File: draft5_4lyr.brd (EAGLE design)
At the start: 120 x 100 mm, 193 parts, among them Q1 Si2333, Q2 2N7002, Q3 2N7002, Q4 2N7002, Q5 2N7002, Q6 2N7002, Q7 2N7002, SW1 TOUCH_PAD-CIRCLE-15MM, SW10 TOUCH_PAD-CIRCLE-15MM, SW4 TOUCH_PAD-CIRCLE-15MM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

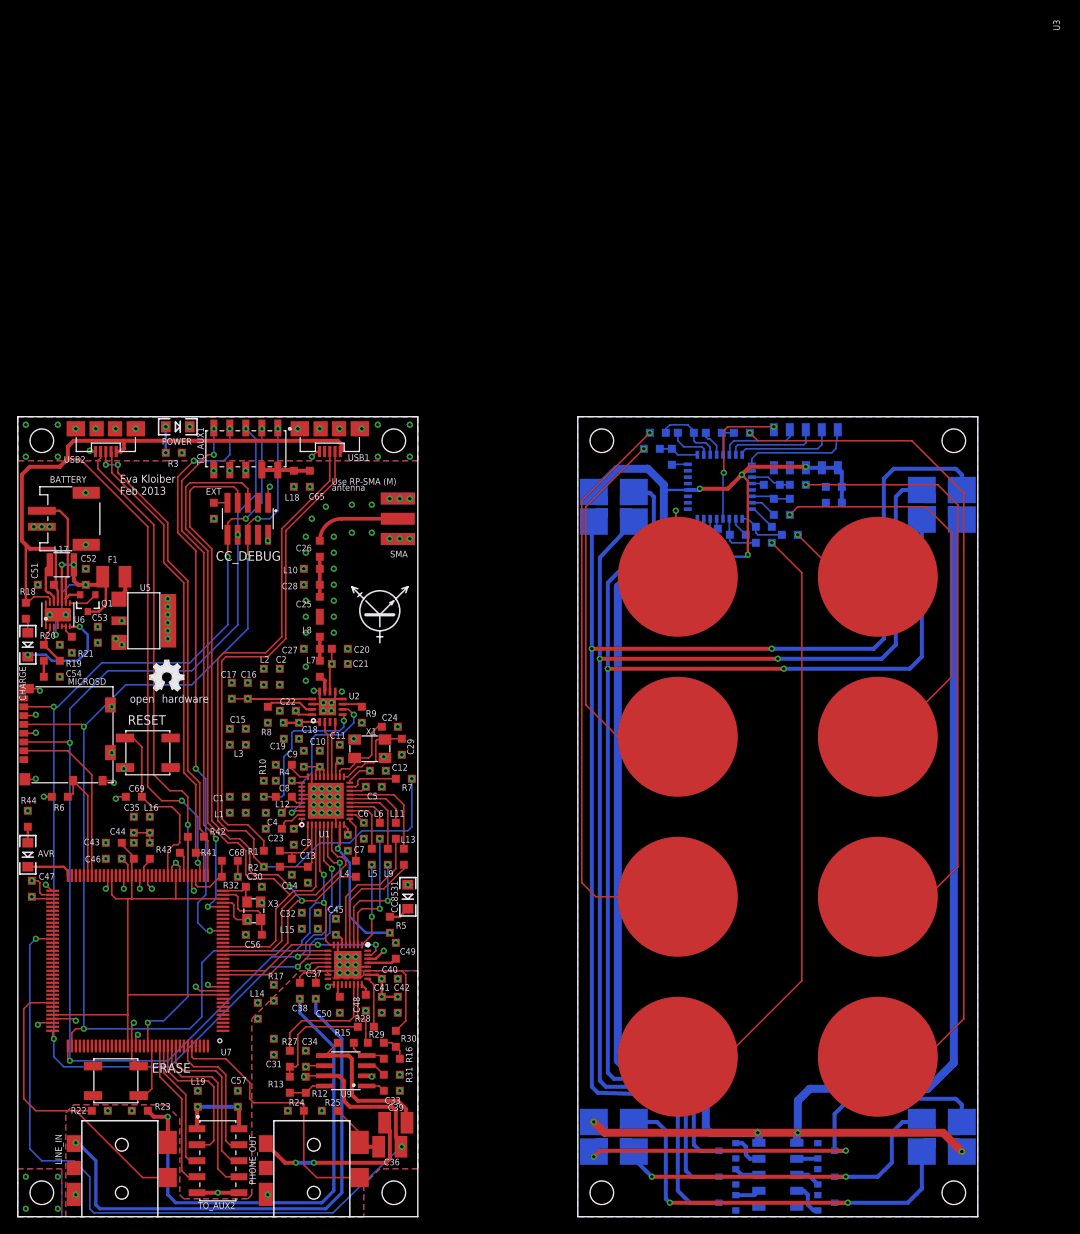
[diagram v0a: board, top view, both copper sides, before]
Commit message: Added JTAG header
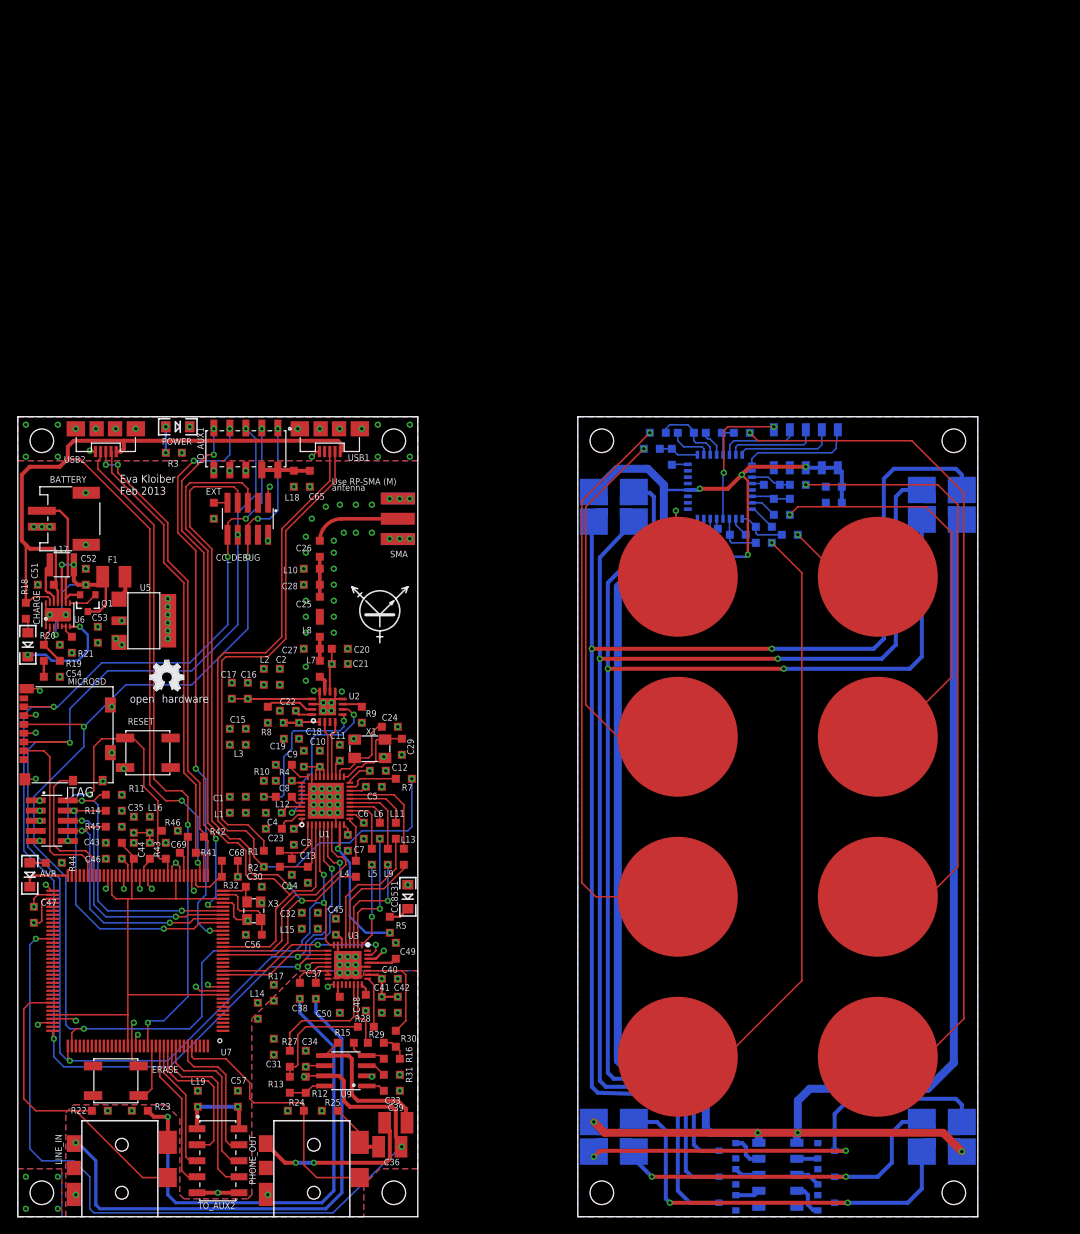
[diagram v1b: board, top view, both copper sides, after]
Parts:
- removed R6: 100K, rcl:R0603
- added JTAG: HEADER-10P-SMD-MALE2, 00-EvaLibrary:HEADER-10P-1.27MM
- added R11, R14, R45, R46: 100K, rcl:R0603
- moved C69 7.85 mm to (18.5, 45.8), turned to 270 degrees
- moved R44 6.39 mm to (4.50, 44.2), turned to 0 degrees
- moved C47 3.26 mm to (2.00, 37.8)
- moved AVR 2.51 mm to (1.50, 42.8)
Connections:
- new net TCK: JTAG.4, R14.1, U7.28
- new net TDI: JTAG.8, R45.1, U7.29
- new net TDO: JTAG.6, U7.30
- new net TMS: JTAG.2, R11.1, U7.31
- net !RESET: now also JTAG.10, R46.1
- net !SD_CARD: now also U7.66; no longer R6.2, U7.67
- net AVR_PWR: now also JTAG.1, R11.2, R14.2, R45.2, R46.2; no longer R6.1
- net CS_SD: now also U7.67; no longer U7.66
- net GND: now also JTAG.3, JTAG.5, JTAG.9
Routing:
- net TCK: track 0.00 -> 36.6 mm, vias 0 -> 2
- net TMS: track 0.00 -> 35.5 mm, vias 0 -> 2
- net TDI: track 0.00 -> 33.0 mm, vias 0 -> 2
- net TDO: track 0.00 -> 30.2 mm, vias 0 -> 2
- net !RESET: track 23.1 -> 39.8 mm, vias 0 -> 2
- net MOSI: track 160.4 -> 167.5 mm
- net SCLK: track 160.7 -> 166.9 mm
- net MISO: track 163.9 -> 168.6 mm
- net !SD_CARD: track 15.0 -> 17.7 mm
- net AVR_PWR: track 31.6 -> 32.1 mm, vias 16 -> 20
- net GND: track 75.9 -> 75.7 mm, vias 167 -> 172

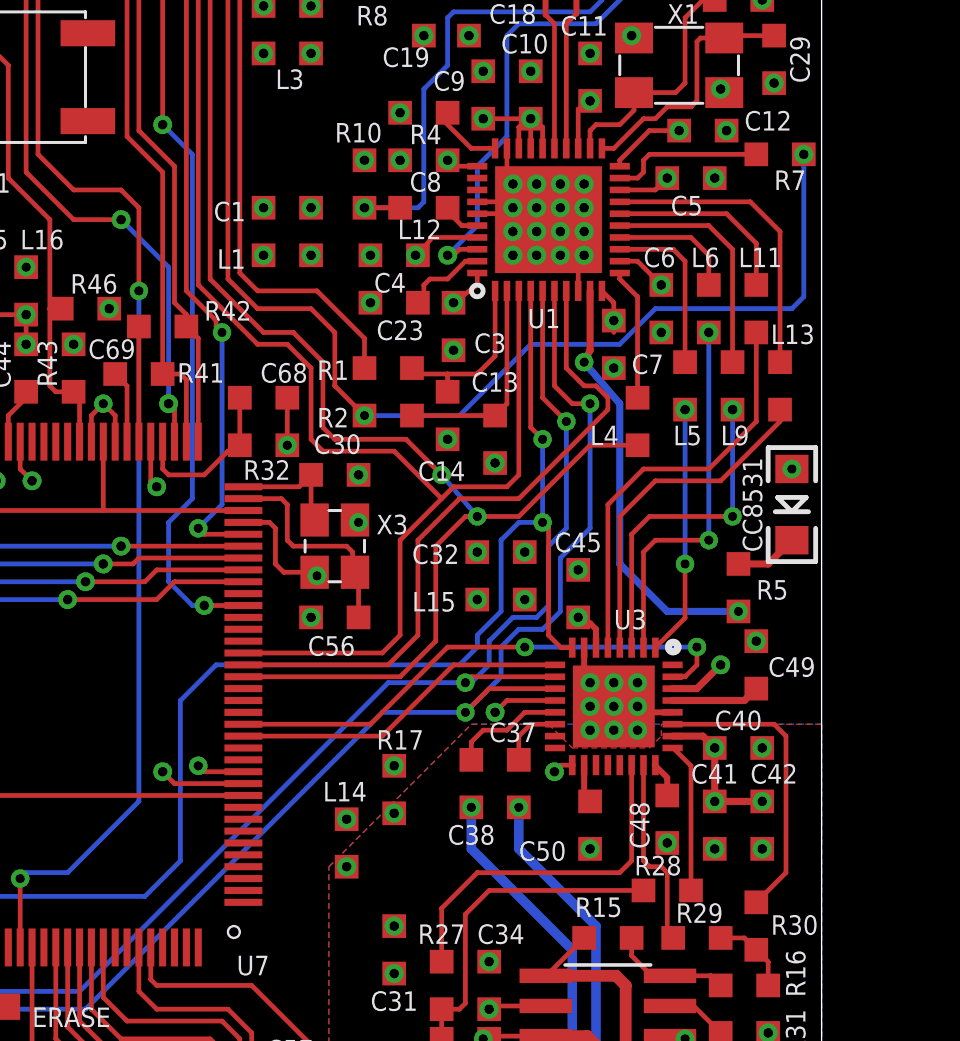
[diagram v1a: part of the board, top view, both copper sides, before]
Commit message: Added USB enumeration sense
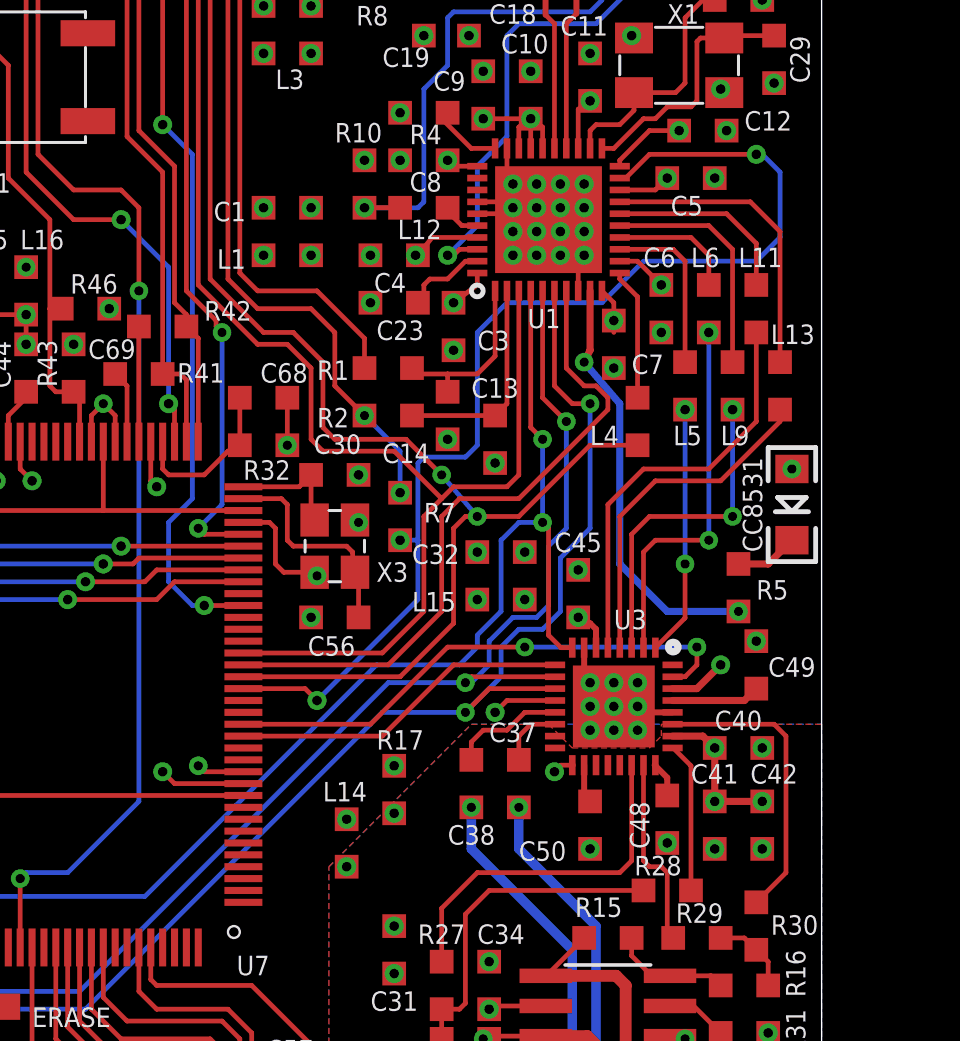
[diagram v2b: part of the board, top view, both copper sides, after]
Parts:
- moved R7 22.1 mm to (32.2, 39.5), turned to 90 degrees
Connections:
- removed net N$24: R7.1, U1.19
- new net USB_SENSE: R7.1, U1.19, U7.19
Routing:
- net USB_SENSE: track 0.00 -> 48.3 mm, vias 0 -> 3
- net D+_CC8531: track 91.0 -> 68.3 mm
- net N$24: track 6.46 -> 0.00 mm
- net SCLK: track 166.9 -> 162.9 mm
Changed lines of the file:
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@@
 </element>
 <element name="C14" library="rcl" package="C0603" value="47p" x="34.25" y="43.75" smashed="yes" rot="R270">
-<attribute name="NAME" x="33" y="41" size="0.82" layer="25" ratio="10"/>
+<attribute name="NAME" x="31.5" y="41.75" size="0.82" layer="25" ratio="10"/>
 </element>
 <element name="C13" library="rcl" package="C0603" value="47p" x="36.25" y="42.75" smashed="yes" rot="R270">
-<attribute name="NAME" x="35.25" y="44.75" size="0.82" layer="25" ratio="10"/>
+<attribute name="NAME" x="35.25" y="44.5" size="0.82" layer="25" ratio="10"/>
 </element>
 <element name="R2" library="rcl" package="R0603" value="33" x="31.75" y="43.75" smashed="yes" rot="R180">
@@
 <attribute name="NAME" x="28.75" y="45.25" size="0.82" layer="25" ratio="10"/>
 </element>
-<element name="R7" library="rcl" package="R0603" value="1.5K" x="48.25" y="54.75" smashed="yes">
-<attribute name="NAME" x="48" y="53.25" size="0.82" layer="25" ratio="10"/>
+<element name="R7" library="rcl" package="R0603" value="1.5K" x="32.25" y="39.5" smashed="yes" rot="R90">
+<attribute name="NAME" x="33.25" y="39.25" size="0.82" layer="25" ratio="10"/>
 </element>
 <element name="X1" library="00-EvaLibrary" package="ABM3C" value="48MHz" x="44" y="58.5" smashed="yes" rot="R180">
@@
 </element>
 <element name="C3" library="rcl" package="C0603" value="1u" x="34.5" y="47.5" smashed="yes" rot="R270">
-<attribute name="NAME" x="35.365" y="46.385" size="0.82" layer="25" ratio="10"/>
+<attribute name="NAME" x="35.5" y="46.5" size="0.82" layer="25" ratio="10"/>
 </element>
 <element name="R17" library="rcl" package="R0603" value="0" x="32" y="28" smashed="yes" rot="R270">
@@
 </element>
 <element name="X3" library="00-EvaLibrary" package="ABM8G" value="12MHz" x="29.5" y="38.25" smashed="yes" rot="R270">
-<attribute name="NAME" x="31.25" y="38.75" size="0.82" layer="25" ratio="10"/>
+<attribute name="NAME" x="31.25" y="36.75" size="0.82" layer="25" ratio="10"/>
 </element>
 <element name="C30" library="00-EvaLibrary" package="C0603" value="10p" x="29.5" y="41.25" smashed="yes">
@@
 <wire x1="36.75" y1="44.25" x2="36.25" y2="43.75" width="0.2" layer="1"/>
 </signal>
-<signal name="N$24">
+<signal name="USB_SENSE">
 <contactref element="R7" pad="1"/>
 <contactref element="U1" pad="19"/>
-<wire x1="47.25" y1="54.75" x2="42.75" y2="54.75" width="0.2" layer="1"/>
-<wire x1="41.5" y1="53.75" x2="42.25" y2="53.75" width="0.2" layer="1"/>
-<wire x1="42.75" y1="54.75" x2="42.5" y2="54.5" width="0.2" layer="1"/>
-<wire x1="42.5" y1="54.5" x2="42.5" y2="54" width="0.2" layer="1"/>
-<wire x1="42.5" y1="54" x2="42.25" y2="53.75" width="0.2" layer="1"/>
+<contactref element="U7" pad="19"/>
+<wire x1="25.65" y1="32.25" x2="28.25" y2="32.25" width="0.2" layer="1"/>
+<wire x1="28.25" y1="32.25" x2="28.75" y2="31.75" width="0.2" layer="1"/>
+<via x="28.75" y="31.75" extent="1-16" drill="0.4"/>
+<wire x1="28.75" y1="31.75" x2="33" y2="36" width="0.2" layer="16"/>
+<wire x1="41.5" y1="53.75" x2="41.75" y2="53.75" width="0.2" layer="1"/>
+<wire x1="41.75" y1="53.75" x2="42.75" y2="54.75" width="0.2" layer="1"/>
+<wire x1="42.75" y1="54.75" x2="47.25" y2="54.75" width="0.2" layer="1"/>
+<via x="47.25" y="54.75" extent="1-16" drill="0.4"/>
+<wire x1="47.25" y1="54.75" x2="47.5" y2="54.75" width="0.2" layer="16"/>
+<wire x1="47.5" y1="54.75" x2="48.25" y2="54" width="0.2" layer="16"/>
+<wire x1="48.25" y1="54" x2="48.25" y2="51.25" width="0.2" layer="16"/>
+<wire x1="48.25" y1="51.25" x2="47.25" y2="50.25" width="0.2" layer="16"/>
+<wire x1="47.25" y1="50.25" x2="42.5" y2="50.25" width="0.2" layer="16"/>
+<wire x1="42.5" y1="50.25" x2="40.75" y2="48.5" width="0.2" layer="16"/>
+<wire x1="40.75" y1="48.5" x2="36.75" y2="48.5" width="0.2" layer="16"/>
+<wire x1="36.75" y1="48.5" x2="35.5" y2="47.25" width="0.2" layer="16"/>
+<wire x1="35.5" y1="47.25" x2="35.5" y2="42.5" width="0.2" layer="16"/>
+<wire x1="35.5" y1="42.5" x2="35" y2="42" width="0.2" layer="16"/>
+<wire x1="35" y1="42" x2="33.25" y2="42" width="0.2" layer="16"/>
+<wire x1="33.25" y1="42" x2="33" y2="41.75" width="0.2" layer="16"/>
+<wire x1="33" y1="41.75" x2="33" y2="38.5" width="0.2" layer="16"/>
+<wire x1="33" y1="38.5" x2="33" y2="36" width="0.2" layer="16"/>
+<wire x1="32.25" y1="38.25" x2="32.25" y2="38.5" width="0.2" layer="1"/>
+<via x="32.25" y="38.5" extent="1-16" drill="0.4"/>
+<wire x1="32.25" y1="38.5" x2="33" y2="38.5" width="0.2" layer="16"/>
 </signal>
 <signal name="MOSI">
@@
 <contactref element="CC_DEBUG" pad="7"/>
 <contactref element="L4" pad="2"/>
-<wire x1="32.25" y1="32.75" x2="33.75" y2="34.25" width="0.2" layer="1"/>
-<wire x1="33.75" y1="34.25" x2="33.75" y2="38.25" width="0.2" layer="1"/>
+<wire x1="32.25" y1="32.75" x2="34.5" y2="35" width="0.2" layer="1"/>
 <wire x1="42.25" y1="42.5" x2="40.25" y2="42.5" width="0.2" layer="1"/>
 <wire x1="40.25" y1="42.5" x2="37.25" y2="39.5" width="0.2" layer="1"/>
@@
 <wire x1="29" y1="43.25" x2="29.5" y2="42.75" width="0.2" layer="1"/>
 <wire x1="29.5" y1="42.75" x2="32.5" y2="42.75" width="0.2" layer="1"/>
-<wire x1="35" y1="39.5" x2="33.75" y2="38.25" width="0.2" layer="1"/>
 <wire x1="32.5" y1="42.75" x2="34" y2="41.25" width="0.2" layer="1"/>
 <via x="34" y="41.25" extent="1-16" drill="0.381"/>
@@
 <contactref element="U7" pad="20"/>
 <wire x1="25.65" y1="32.75" x2="32.25" y2="32.75" width="0.2" layer="1"/>
+<wire x1="34.5" y1="35" x2="34.5" y2="39" width="0.2" layer="1"/>
+<wire x1="34.5" y1="39" x2="35" y2="39.5" width="0.2" layer="1"/>
 </signal>
 <signal name="N$9">
@@
 <wire x1="37.25" y1="49" x2="37.25" y2="41.25" width="0.2" layer="1"/>
 <wire x1="25.65" y1="33.75" x2="31.5" y2="33.75" width="0.2" layer="1"/>
-<wire x1="31.5" y1="33.75" x2="32.25" y2="34.5" width="0.2" layer="1"/>
-<wire x1="32.25" y1="34.5" x2="32.25" y2="38.5" width="0.2" layer="1"/>
-<wire x1="32.25" y1="38.5" x2="34" y2="40.25" width="0.2" layer="1"/>
 <wire x1="34" y1="40.25" x2="34.5" y2="40.75" width="0.2" layer="1"/>
 <wire x1="34.5" y1="40.75" x2="36.75" y2="40.75" width="0.2" layer="1"/>
@@
 <wire x1="29" y1="42.25" x2="32" y2="42.25" width="0.2" layer="1"/>
 <wire x1="32" y1="42.25" x2="34" y2="40.25" width="0.2" layer="1"/>
+<wire x1="31.5" y1="33.75" x2="33.25" y2="35.5" width="0.2" layer="1"/>
+<wire x1="33.25" y1="35.5" x2="33.25" y2="39.5" width="0.2" layer="1"/>
+<wire x1="33.25" y1="39.5" x2="34" y2="40.25" width="0.2" layer="1"/>
 </signal>
 <signal name="CS_CODEC">
@@
 <wire x1="35.5" y1="34.5" x2="35.5" y2="34" width="0.2" layer="16"/>
 <wire x1="35.5" y1="34" x2="34.75" y2="33.25" width="0.2" layer="16"/>
-<wire x1="34.75" y1="33.25" x2="24.5" y2="33.25" width="0.2" layer="16"/>
-<wire x1="24.5" y1="33.25" x2="23" y2="31.75" width="0.2" layer="16"/>
-<wire x1="23" y1="31.75" x2="23" y2="25" width="0.2" layer="16"/>
-<wire x1="23" y1="25" x2="21.5" y2="23.5" width="0.2" layer="16"/>
+<wire x1="34.75" y1="33.25" x2="31.25" y2="33.25" width="0.2" layer="16"/>
+<wire x1="31.25" y1="33.25" x2="21.5" y2="23.5" width="0.2" layer="16"/>
 <wire x1="39.5" y1="33.975" x2="39.025" y2="33.975" width="0.2" layer="1"/>
 <wire x1="39.025" y1="33.975" x2="38.5" y2="34.5" width="0.2" layer="1"/>
@@
 <contactref element="USB1" pad="3"/>
 <contactref element="R7" pad="2"/>
-<via x="49.25" y="54.75" extent="1-16" drill="0.4"/>
-<wire x1="49.25" y1="54.75" x2="49.25" y2="48.75" width="0.2" layer="16"/>
-<wire x1="49.25" y1="48.75" x2="48.75" y2="48.25" width="0.2" layer="16"/>
-<wire x1="48.75" y1="48.25" x2="43" y2="48.25" width="0.2" layer="16"/>
-<wire x1="43" y1="48.25" x2="41.5" y2="46.75" width="0.2" layer="16"/>
-<wire x1="41.5" y1="46.75" x2="37.75" y2="46.75" width="0.2" layer="16"/>
-<wire x1="37.75" y1="46.75" x2="34.75" y2="43.75" width="0.2" layer="16"/>
-<wire x1="34.75" y1="43.75" x2="30.75" y2="43.75" width="0.2" layer="16"/>
 <via x="30.75" y="43.75" extent="1-16" drill="0.381"/>
 <wire x1="39" y1="95.65" x2="39" y2="92" width="0.2" layer="1"/>
@@
 <wire x1="29.5" y1="47.25" x2="29.5" y2="45" width="0.2" layer="1"/>
 <wire x1="29.5" y1="45" x2="30.75" y2="43.75" width="0.2" layer="1"/>
+<via x="32.25" y="40.5" extent="1-16" drill="0.4"/>
+<wire x1="32.25" y1="40.5" x2="32.25" y2="42.25" width="0.2" layer="16"/>
+<wire x1="32.25" y1="42.25" x2="30.75" y2="43.75" width="0.2" layer="16"/>
 </signal>
 <signal name="D-_CC8531">
@@
 <contactref element="U7" pad="21"/>
 <wire x1="25.65" y1="33.25" x2="31.75" y2="33.25" width="0.2" layer="1"/>
-<wire x1="31.75" y1="33.25" x2="33" y2="34.5" width="0.2" layer="1"/>
-<wire x1="33" y1="34.5" x2="33" y2="38.5" width="0.2" layer="1"/>
-<wire x1="33" y1="38.5" x2="34.75" y2="40.25" width="0.2" layer="1"/>
+<wire x1="31.75" y1="33.25" x2="34" y2="35.5" width="0.2" layer="1"/>
 <wire x1="34.75" y1="40.25" x2="37.25" y2="40.25" width="0.2" layer="1"/>
 <wire x1="37.25" y1="40.25" x2="41" y2="44" width="0.2" layer="1"/>
@@
 <wire x1="40" y1="45" x2="39.25" y2="45.75" width="0.2" layer="1"/>
 <wire x1="39.25" y1="45.75" x2="39.25" y2="49" width="0.2" layer="1"/>
+<wire x1="34" y1="35.5" x2="34" y2="39.5" width="0.2" layer="1"/>
+<wire x1="34" y1="39.5" x2="34.75" y2="40.25" width="0.2" layer="1"/>
 </signal>
 <signal name="AUX_RED_TOP">

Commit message: Fixed stuff, created prototype board
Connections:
- new net M_BLCK: U7.7
- new net M_DIN/S_DOUT: U7.89
- new net M_DOUT/S_DIN: U7.78
- new net M_WCLK: U7.8
- new net S_BCLK: U7.90
- new net S_WCLK: U7.88
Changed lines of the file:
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@@
 <wire x1="11" y1="50.75" x2="7" y2="50.75" width="0.2" layer="1"/>
+</signal>
+<signal name="M_BLCK">
+<contactref element="U7" pad="7"/>
+</signal>
+<signal name="M_WCLK">
+<contactref element="U7" pad="8"/>
+</signal>
+<signal name="M_DOUT/S_DIN">
+<contactref element="U7" pad="78"/>
+</signal>
+<signal name="S_WCLK">
+<contactref element="U7" pad="88"/>
+</signal>
+<signal name="M_DIN/S_DOUT">
+<contactref element="U7" pad="89"/>
+</signal>
+<signal name="S_BCLK">
+<contactref element="U7" pad="90"/>
 </signal>
 </signals>
